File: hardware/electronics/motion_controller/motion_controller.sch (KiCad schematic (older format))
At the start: 186 parts, among them K1 CONN_3, K10 CONN_3, K11 CONN_3, K12 CONN_3, K13 CONN_3, K14 CONN_3, K15 CONN_3, K2 CONN_3, K3 CONN_3, K4 CONN_3, K5 CONN_3, K6 CONN_3, K7 CONN_3, K8 CONN_3, K9 CONN_3, P1 CONN_2, P10 CONN_4, P11 CONN_4, P12 CONN_4, P13 CONN_2, P14 CONN_2, P15 CONN_2, P16 CONN_2, P17 CONN_2, P18 CONN_2, P19 CONN_2X2, P2 CONN_5X2, P20 CONN_2X2, P21 CONN_2, P22 CONN_2, P23 CONN_2, P24 CONN_2, P25 CONN_2, P26 CONN_2X2, P27 CONN_2, P28 CONN_2, P29 CONN_2, P3 CONN_2X2, P30 CONN_1, P31 CONN_1, P32 CONN_1, P33 CONN_1, P4 CONN_2, P5 CONN_34X2, P6 CONN_4, P7 CONN_4, P8 CONN_4, P9 CONN_4, U1 TEENSY3.1, U10 OP07, U11 OP07, U12 OP07, U13 OP07, U14 OP07, U15 OP07, U16 OP07, U17 MEA1D0512SC, U18 PJRC_SD_CARD, U2 NC7WZ04, U3 NC7WZ16, U4 NC7WZ16, U5 SSR_DC_6PIN, U6 MAX6176AASA+, U7 OP07, U8 OP07, U9 OP07

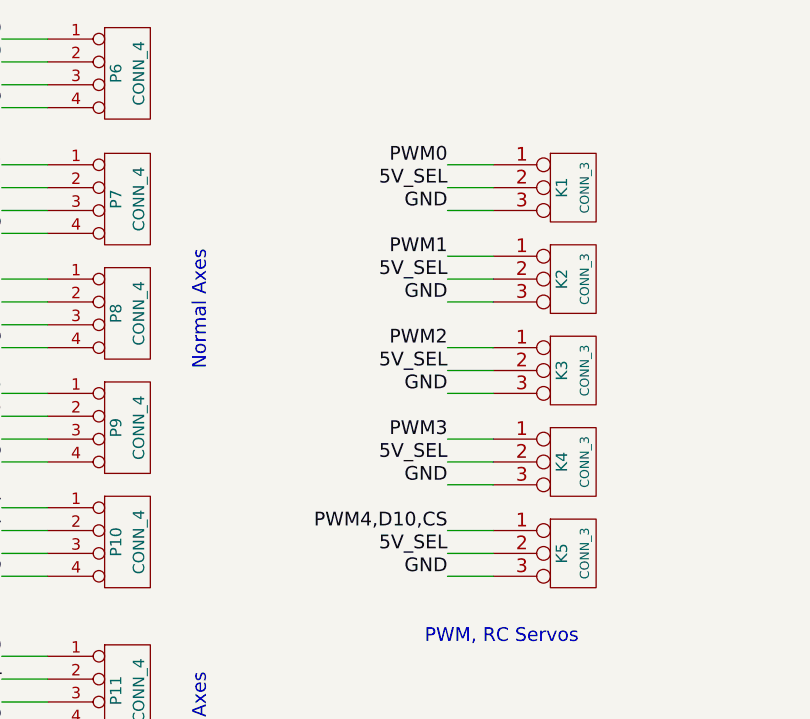
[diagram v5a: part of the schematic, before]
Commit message: Finished preliminary routing of motion controller PCB.
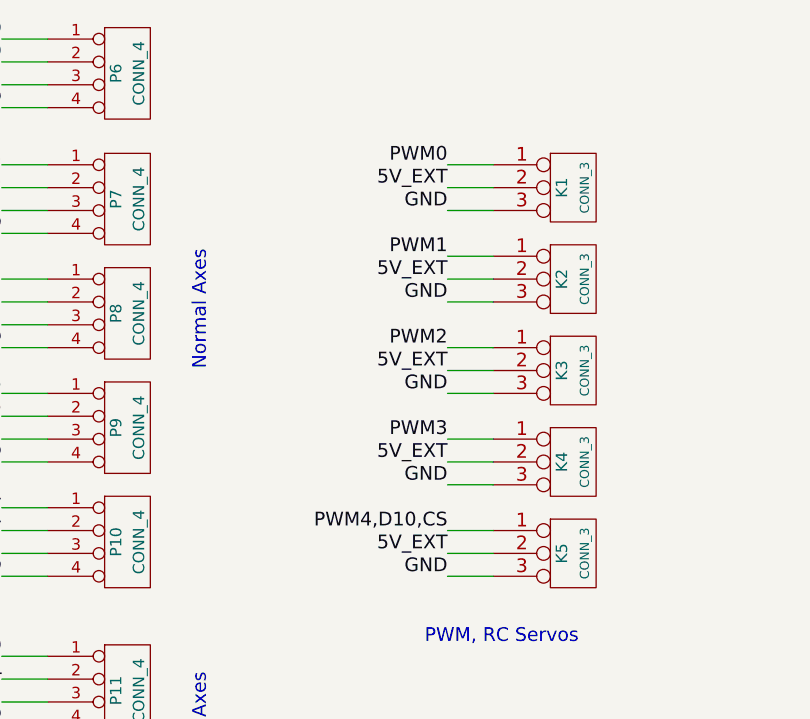
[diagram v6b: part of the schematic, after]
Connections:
- net 5V_EXT: now also K1.2 (PM), K2.2 (PM), K3.2 (PM), K4.2 (PM), K5.2 (PM)
- net 5V_SEL: no longer K1.2 (PM), K2.2 (PM), K3.2 (PM), K4.2 (PM), K5.2 (PM)
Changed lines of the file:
@@
 GND
 Text Label 3400 4850 2    60   ~ 0
-5V_SEL
+5V_EXT
 Text Label 3400 4750 2    60   ~ 0
 PWM0
@@
 GND
 Text Label 3400 5250 2    60   ~ 0
-5V_SEL
+5V_EXT
 Text Label 3400 5150 2    60   ~ 0
 PWM1
@@
 GND
 Text Label 3400 5650 2    60   ~ 0
-5V_SEL
+5V_EXT
 Text Label 3400 5550 2    60   ~ 0
 PWM2
@@
 GND
 Text Label 3400 6050 2    60   ~ 0
-5V_SEL
+5V_EXT
 Text Label 3400 5950 2    60   ~ 0
 PWM3
@@
 GND
 Text Label 3400 6450 2    60   ~ 0
-5V_SEL
+5V_EXT
 Text Label 3400 6350 2    60   ~ 0
 PWM4,D10,CS

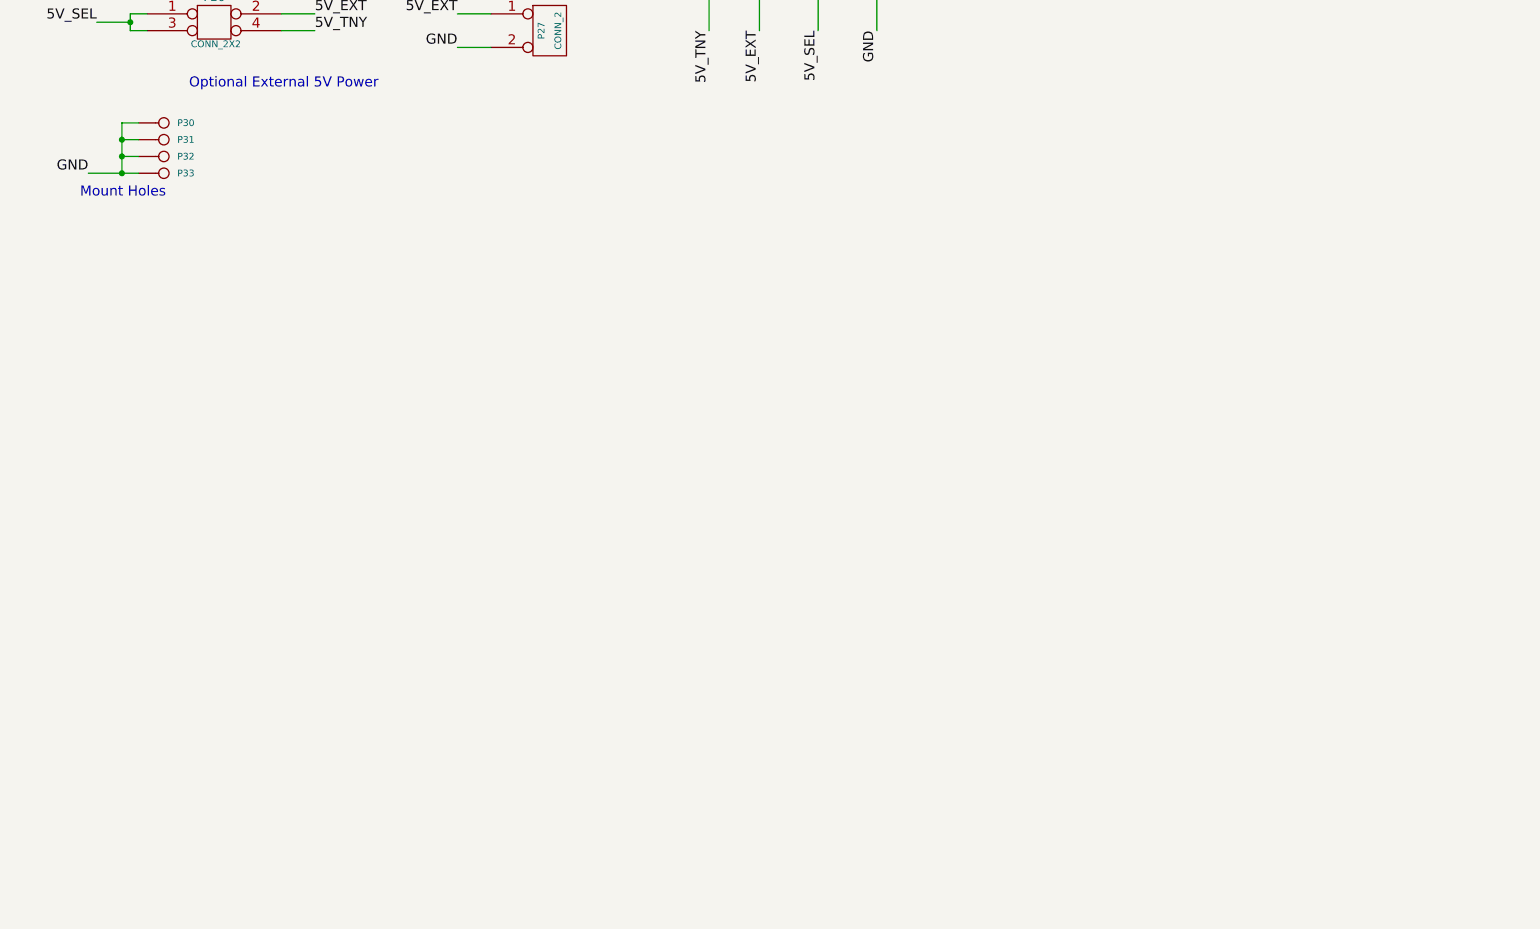
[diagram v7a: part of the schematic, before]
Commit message: Modified motion controller pcb slightly - made so that only one mounting hole is grounded.
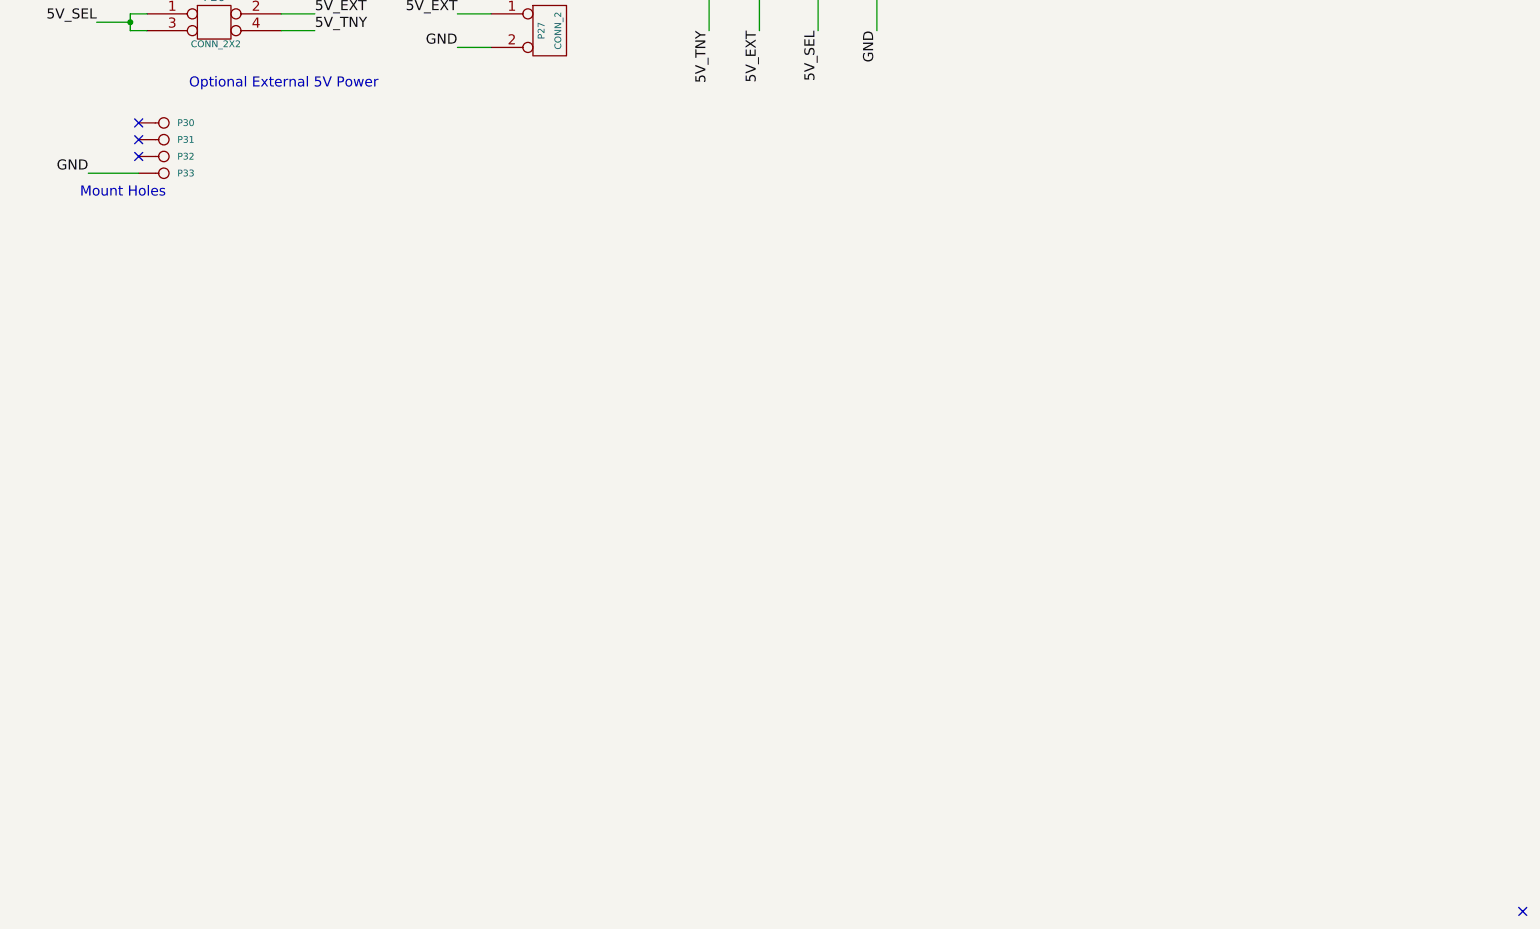
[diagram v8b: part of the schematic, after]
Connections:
- net GND: no longer P30.1, P31.1, P32.1
- no-connect marks 92 -> 96
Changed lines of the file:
@@
 5V_TNY
-$Comp
-L CONN_1 P30
-U 1 1 57085C98
-P 12800 13350
-F 0 "P30" H 12880 13350 40  0000 L CNN
-F 1 "CONN_1" H 12800 13405 30  0001 C CNN
-F 2 "" H 12800 13350 60  0000 C CNN
-F 3 "" H 12800 13350 60  0000 C CNN
-	1    12800 13350
-	1    0    0    -1
-$EndComp
 $Comp
 L CONN_1 P31
@@
 $EndComp
 Wire Wire Line
-	12650 13350 12550 13350
-Wire Wire Line
-	12550 13350 12550 13650
-Wire Wire Line
 	12350 13650 12650 13650
-Wire Wire Line
-	12650 13450 12550 13450
-Connection ~ 12550 13450
-Wire Wire Line
-	12650 13550 12550 13550
-Connection ~ 12550 13550
-Connection ~ 12550 13650
 Text Label 12350 13650 2    60   ~ 0
 GND
 Text Notes 12300 13800 0    60   ~ 0
 Mount Holes
+$Comp
+L CONN_1 P30
+U 1 1 57085C98
+P 12800 13350
+F 0 "P30" H 12880 13350 40  0000 L CNN
+F 1 "CONN_1" H 12800 13405 30  0001 C CNN
+F 2 "" H 12800 13350 60  0000 C CNN
+F 3 "" H 12800 13350 60  0000 C CNN
+	1    12800 13350
+	1    0    0    -1
+$EndComp
+NoConn ~ 12650 13350
+NoConn ~ 12650 13450
+NoConn ~ 12650 13550
+NoConn ~ 20900 18050
 $EndSCHEMATC
